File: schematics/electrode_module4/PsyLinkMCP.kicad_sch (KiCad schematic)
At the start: 64 parts

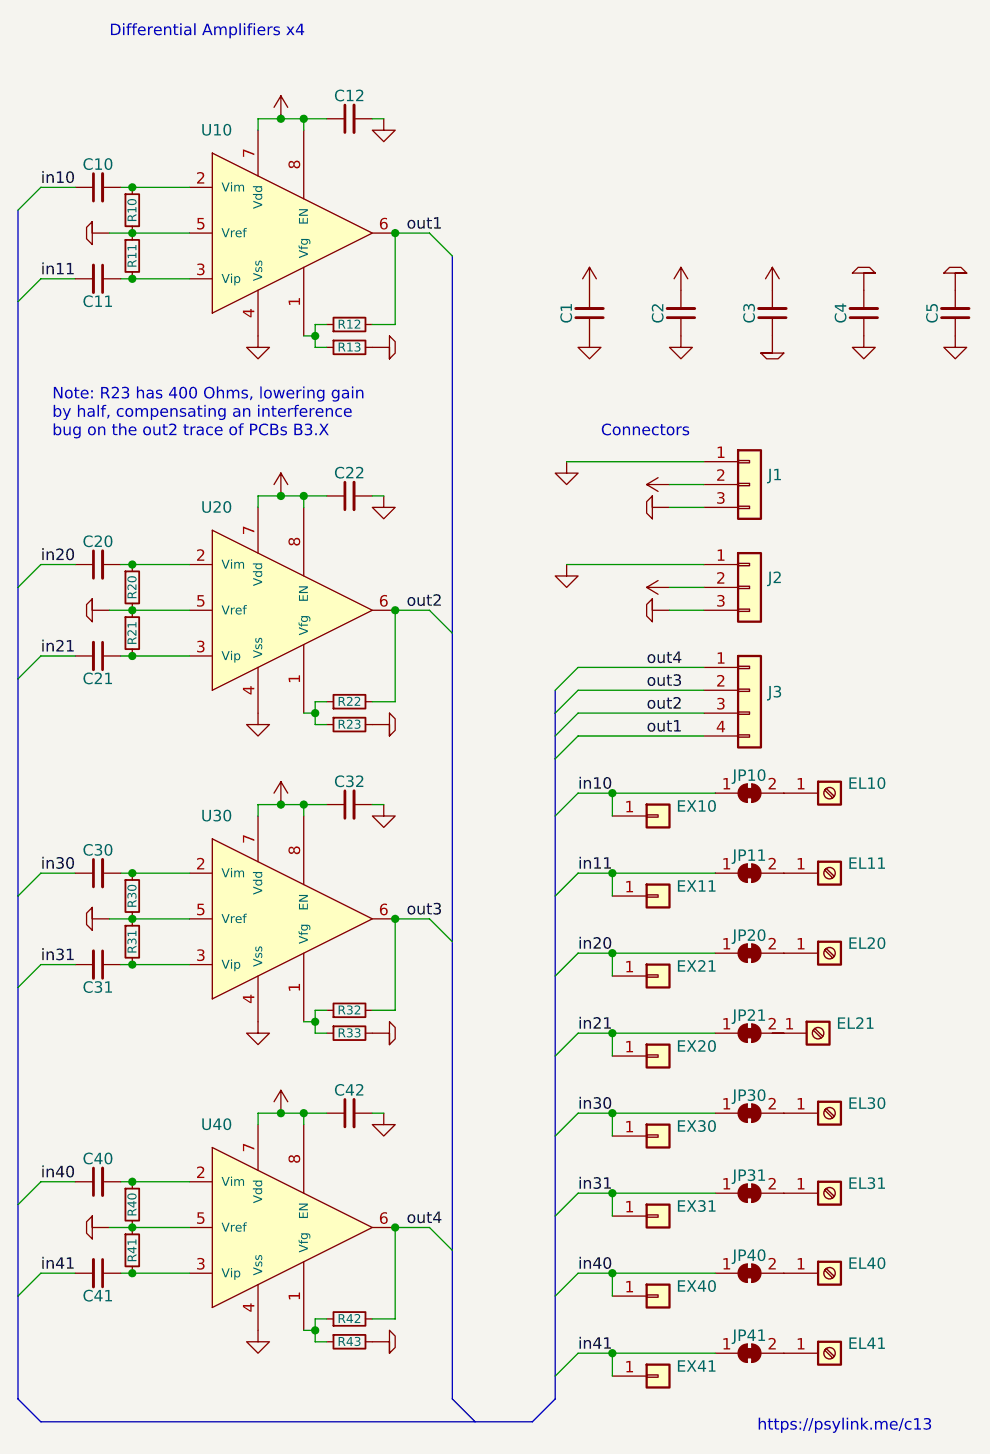
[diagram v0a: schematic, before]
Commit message: removed unneeded "bug fix" of lowering gain by half on 2nd output
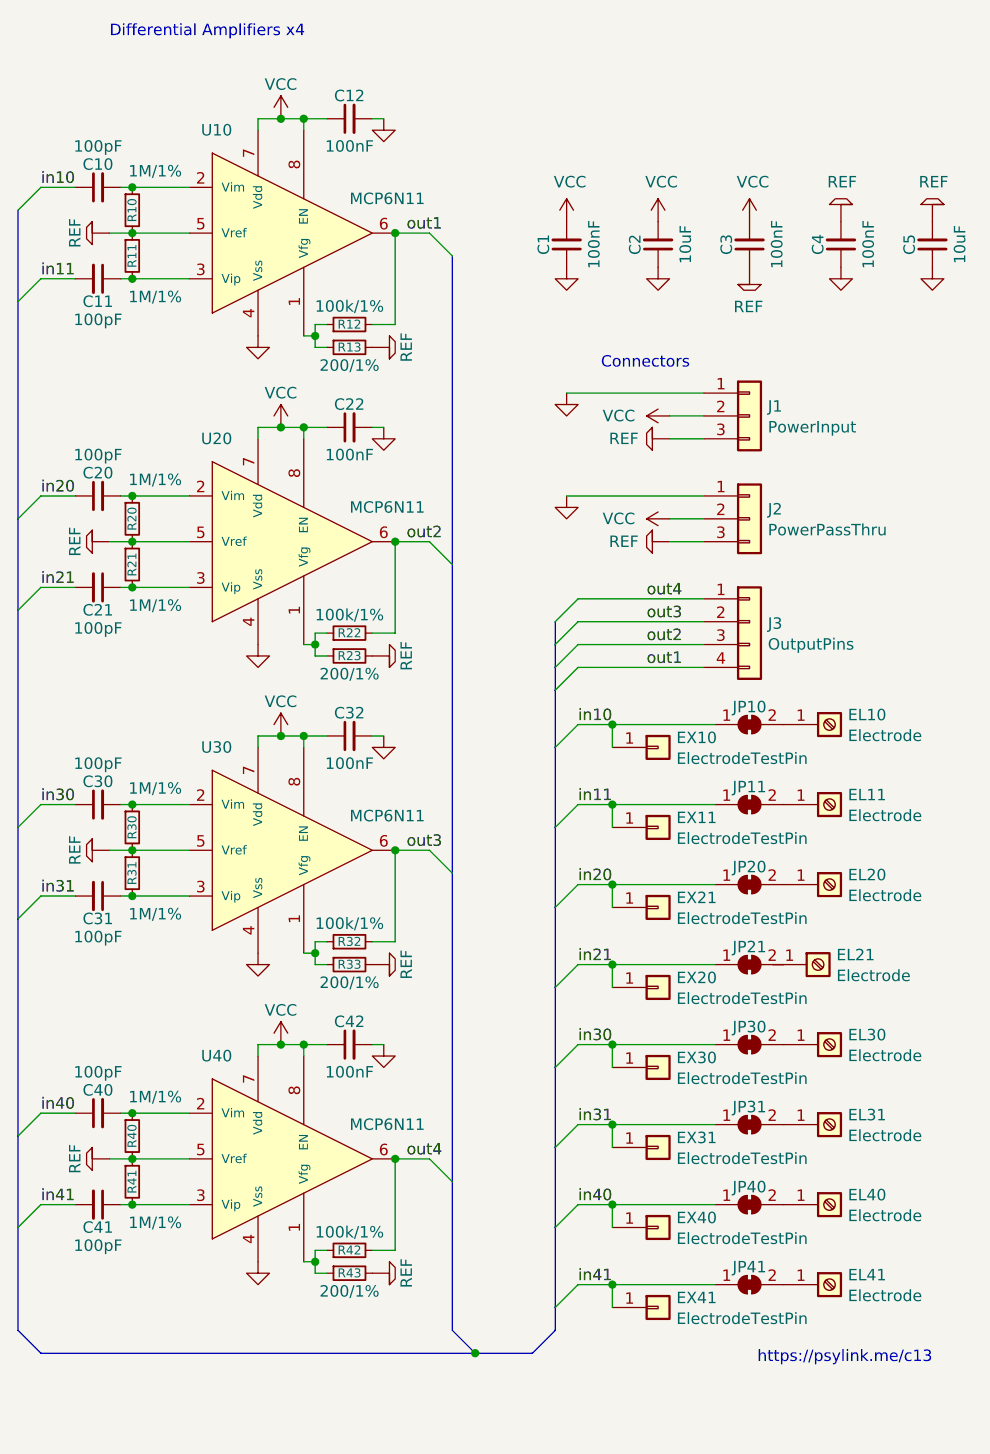
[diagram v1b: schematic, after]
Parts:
- C1, C12, C22, C3, C32, C4, C42: value (none) -> 100nF; footprint (none) -> Capacitor_SMD:C_0805_2012Metric_Pad1.15x1.40mm_HandSolder
- C10, C11, C20, C21, C30, C31, C40, C41: value (none) -> 100pF; footprint (none) -> Capacitor_SMD:C_0805_2012Metric_Pad1.15x1.40mm_HandSolder
- C2, C5: value (none) -> 10uF; footprint (none) -> Capacitor_SMD:C_0805_2012Metric_Pad1.15x1.40mm_HandSolder
- EL10, EL11, EL20, EL21, EL30, EL31, EL40, EL41: value (none) -> Electrode; footprint (none) -> MountingHole:MountingHole_3.7mm_Pad
- EX10, EX11, EX20, EX21, EX30, EX31, EX40, EX41: value (none) -> ElectrodeTestPin; footprint (none) -> Connector_PinHeader_2.54mm:PinHeader_1x01_P2.54mm_Vertical
- J1: value (none) -> PowerInput; footprint (none) -> Connector_PinHeader_2.54mm:PinHeader_1x03_P2.54mm_Vertical
- J2: value (none) -> PowerPassThru; footprint (none) -> Connector_PinHeader_2.54mm:PinHeader_1x03_P2.54mm_Vertical
- J3: value (none) -> OutputPins; footprint (none) -> Connector_PinHeader_2.54mm:PinHeader_1x04_P2.54mm_Vertical
- JP10, JP11, JP20, JP21, JP30, JP31, JP40, JP41: value (none) -> SolderJumper_2_Bridged; footprint (none) -> Jumper:SolderJumper-2_P1.3mm_Bridged_RoundedPad1.0x1.5mm
- R10, R11, R20, R21, R30, R31, R40, R41: value (none) -> 1M/1%; footprint (none) -> Resistor_SMD:R_0805_2012Metric_Pad1.15x1.40mm_HandSolder
- R12, R22, R32, R42: value (none) -> 100k/1%; footprint (none) -> Resistor_SMD:R_0805_2012Metric_Pad1.15x1.40mm_HandSolder
- R13, R23, R33, R43: value (none) -> 200/1%; footprint (none) -> Resistor_SMD:R_0805_2012Metric_Pad1.15x1.40mm_HandSolder
- U10, U20, U30, U40: value (none) -> MCP6N11; footprint (none) -> Package_SO:SOIC-8_3.9x4.9mm_P1.27mm
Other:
- note removed: "Note: R23 has 400 Ohms, lowering gain by half, compensating an interference bug on the out2 trace of PCBs B3.X"
- moved on the sheet: C1, C2, C20, C21, C22, C3, C30, C31, C32, C4, C40, C41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
